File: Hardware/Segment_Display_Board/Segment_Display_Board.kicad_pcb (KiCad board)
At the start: 2 copper layers, 58.4 x 141 mm, 91 parts, among them J101 IN, J102 OUT, J301 USB_B_Micro, J302 PROG, J401 19V Input, J501 Bottom Conn, J502 Top Conn, Q1001 MMBT3904, Q1002 MMBT3906, Q1101 MMBT3904, Q1102 MMBT3906, Q1201 MMBT3904, Q1202 MMBT3906, Q601 MMBT3904, Q602 MMBT3906, Q701 MMBT3904, Q702 MMBT3906, Q801 MMBT3904, Q802 MMBT3906, Q901 MMBT3904, Q902 MMBT3906, SW201 RESET, SW202 DAY_RESET, SW203 DAY_ADV, SW204 DAY_SUB, U201 ATmega328P-A, U202 DS1307Z+, U301 FT232RL, U401 NCV1117ST50T3G, U501 SN74HC595, Y201 16mHz, Y202 32.768kHz

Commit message: Fixup some stuff
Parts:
- R1003, R1103, R1203, R603, R703, R803, R903: value 240R -> 270R
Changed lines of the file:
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@@
       (effects (font (size 0.75 0.75) (thickness 0.15)))
     )
-    (fp_text value "240R" (at 0 2.5) (layer "F.Fab")
+    (fp_text value "270R" (at 0 2.5) (layer "F.Fab")
       (effects (font (size 1 1) (thickness 0.15)))
     )
@@
       (effects (font (size 0.75 0.75) (thickness 0.15)))
     )
-    (fp_text value "240R" (at 0 2.5) (layer "F.Fab")
+    (fp_text value "270R" (at 0 2.5) (layer "F.Fab")
       (effects (font (size 1 1) (thickness 0.15)))
     )
@@
       (effects (font (size 0.75 0.75) (thickness 0.15)))
     )
-    (fp_text value "240R" (at 0 2.5) (layer "F.Fab")
+    (fp_text value "270R" (at 0 2.5) (layer "F.Fab")
       (effects (font (size 1 1) (thickness 0.15)))
     )
@@
       (effects (font (size 0.75 0.75) (thickness 0.15)))
     )
-    (fp_text value "240R" (at 0 2.5) (layer "F.Fab")
+    (fp_text value "270R" (at 0 2.5) (layer "F.Fab")
       (effects (font (size 1 1) (thickness 0.15)))
     )
@@
       (effects (font (size 0.75 0.75) (thickness 0.15)))
     )
-    (fp_text value "240R" (at 0 2.5) (layer "F.Fab")
+    (fp_text value "270R" (at 0 2.5) (layer "F.Fab")
       (effects (font (size 1 1) (thickness 0.15)))
     )
@@
       (effects (font (size 0.75 0.75) (thickness 0.15)))
     )
-    (fp_text value "240R" (at 0 2.5) (layer "F.Fab")
+    (fp_text value "270R" (at 0 2.5) (layer "F.Fab")
       (effects (font (size 1 1) (thickness 0.15)))
     )
@@
       (effects (font (size 0.75 0.75) (thickness 0.15)))
     )
-    (fp_text value "240R" (at 0 2.5) (layer "F.Fab")
+    (fp_text value "270R" (at 0 2.5) (layer "F.Fab")
       (effects (font (size 1 1) (thickness 0.15)))
     )

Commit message: Works enough to do something basic
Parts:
- R1003, R1103, R1203, R603, R703, R803, R903: value 270R -> 680R
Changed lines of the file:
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@@
       (effects (font (size 0.75 0.75) (thickness 0.15)))
     )
-    (fp_text value "270R" (at 0 2.5) (layer "F.Fab")
+    (fp_text value "680R" (at 0 2.5) (layer "F.Fab")
       (effects (font (size 1 1) (thickness 0.15)))
     )
@@
       (effects (font (size 0.75 0.75) (thickness 0.15)))
     )
-    (fp_text value "270R" (at 0 2.5) (layer "F.Fab")
+    (fp_text value "680R" (at 0 2.5) (layer "F.Fab")
       (effects (font (size 1 1) (thickness 0.15)))
     )
@@
       (effects (font (size 0.75 0.75) (thickness 0.15)))
     )
-    (fp_text value "270R" (at 0 2.5) (layer "F.Fab")
+    (fp_text value "680R" (at 0 2.5) (layer "F.Fab")
       (effects (font (size 1 1) (thickness 0.15)))
     )
@@
       (effects (font (size 0.75 0.75) (thickness 0.15)))
     )
-    (fp_text value "270R" (at 0 2.5) (layer "F.Fab")
+    (fp_text value "680R" (at 0 2.5) (layer "F.Fab")
       (effects (font (size 1 1) (thickness 0.15)))
     )
@@
       (effects (font (size 0.75 0.75) (thickness 0.15)))
     )
-    (fp_text value "270R" (at 0 2.5) (layer "F.Fab")
+    (fp_text value "680R" (at 0 2.5) (layer "F.Fab")
       (effects (font (size 1 1) (thickness 0.15)))
     )
@@
       (effects (font (size 0.75 0.75) (thickness 0.15)))
     )
-    (fp_text value "270R" (at 0 2.5) (layer "F.Fab")
+    (fp_text value "680R" (at 0 2.5) (layer "F.Fab")
       (effects (font (size 1 1) (thickness 0.15)))
     )
@@
       (effects (font (size 0.75 0.75) (thickness 0.15)))
     )
-    (fp_text value "270R" (at 0 2.5) (layer "F.Fab")
+    (fp_text value "680R" (at 0 2.5) (layer "F.Fab")
       (effects (font (size 1 1) (thickness 0.15)))
     )

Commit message: Include battery info
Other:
- board text added: "Fits - DL2020 - CR2025 - CR2032"
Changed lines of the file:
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@@
     (effects (font (size 1.5 1.5) (thickness 0.3)))
+  )
+  (gr_text "Fits\n - DL2020\n - CR2025\n - CR2032" (at 143.5 56.5) (layer "F.SilkS")
+    (effects (font (size 1 1) (thickness 0.15)) (justify left))
   )
   (segment (start 127.665 138.335) (end 127.665 130.835) (width 2) (layer "F.Cu") (net 1))

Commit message: Include fancy ICSP programmer (lol)
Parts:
- added J201: Tag Connect, Connector:Tag-Connect_TC2050-IDC-FP_2x05_P1.27mm_Vertical, F.Cu at (147.0, 94.0)
- added JP201: RSTBridge, Jumper:SolderJumper-2_P1.3mm_Bridged_Pad1.0x1.5mm, F.Cu at (139.0, 94.5)
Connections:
- net Net-(D201-Pad2) renamed /MCU/ICSP_SCK
- U201 pad 15: unconnected-(U201-Pad15) -> /MCU/ICSP_MOSI
- U201 pad 16: unconnected-(U201-Pad16) -> /MCU/ICSP_MISO
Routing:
- net /MCU/ICSP_MOSI: track 0.00 -> 23.1 mm, vias 0 -> 2
- net /MCU/ICSP_MISO: track 0.00 -> 15.9 mm, vias 0 -> 2
- net /MCU/ICSP_RST: track 0.00 -> 15.5 mm, vias 0 -> 2
- net /MCU/ICSP_SCK: track 6.80 -> 19.7 mm
- net +5V: track 298.6 -> 306.3 mm, vias 14 -> 15
- net /MCU/RST: track 29.5 -> 37.1 mm
- net GND: track 23.0 -> 24.6 mm, vias 21 -> 33

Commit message: Use new 5in symbol and footprint
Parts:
- removed J501: Bottom Conn, Connector_PinSocket_2.54mm:PinSocket_1x09_P2.54mm_Vertical
- removed J502: Top Conn, Connector_PinSocket_2.54mm:PinSocket_1x09_P2.54mm_Vertical
- added U501: 5inSegment, KenwoodFox:5inSegment, F.Cu at (157.0, 92.0)
- renumbered U501 to U502
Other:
- board text removed: "A"
- board text removed: "B"
- board text removed: "C"
- board text removed: "D"
- board text removed: "DP"
- board text removed: "E"
- board text removed: "F"
- board text removed: "G"
- board text removed: "GND"

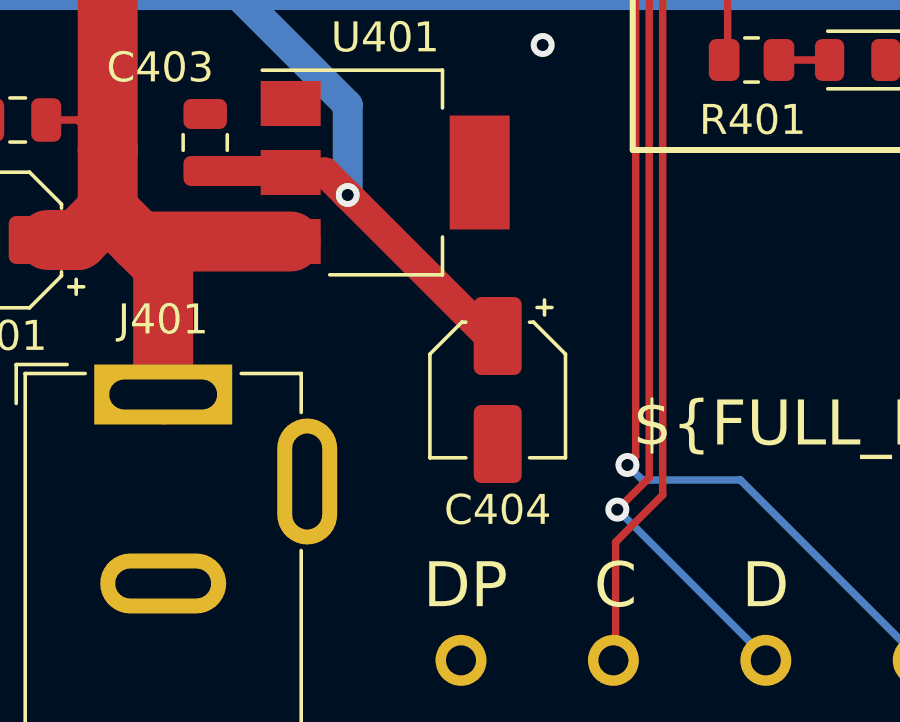
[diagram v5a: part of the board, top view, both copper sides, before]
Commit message: Change package for 1uF capacitor
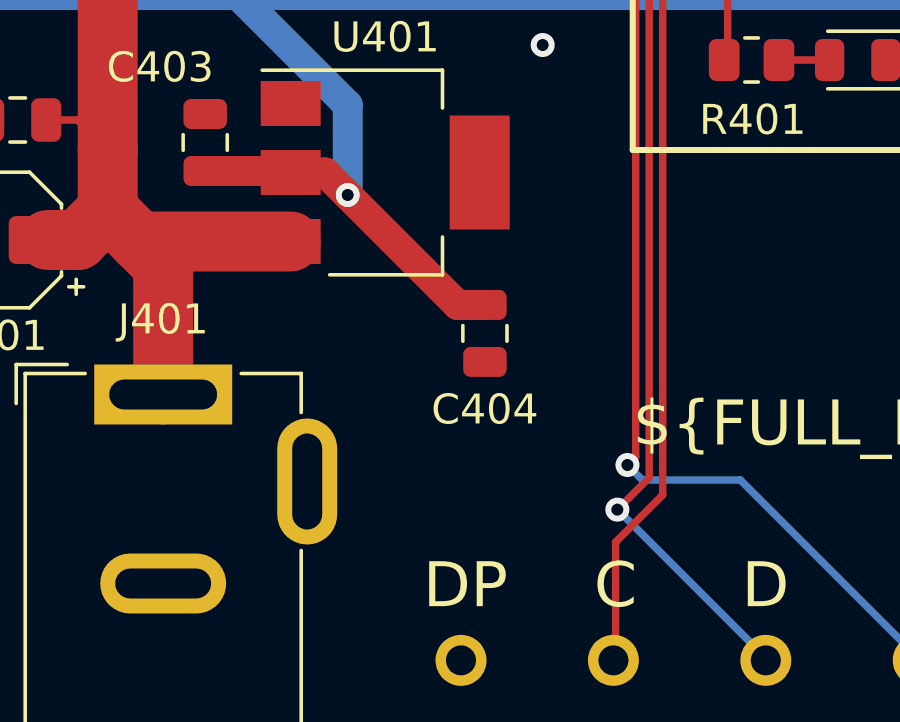
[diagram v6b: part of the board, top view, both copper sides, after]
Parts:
- C404: value 1uf -> 1uF; footprint Capacitor_SMD:CP_Elec_4x3 -> Capacitor_SMD:C_0805_2012Metric
- moved C404 1.93 mm to (147.6, 150.1)
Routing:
- net +5V: track 306.3 -> 305.4 mm
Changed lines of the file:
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@@
       (connect_pads (clearance 0))
       (min_thickness 0.254)
-      (keepout (tracks allowed) (vias not_allowed) (pads allowed ) (copperpour not_allowed) (footprints not_allowed))
+      (keepout (tracks allowed) (vias not_allowed) (pads allowed) (copperpour not_allowed) (footprints not_allowed))
       (fill (thermal_gap 0.508) (thermal_bridge_width 0.508))
       (polygon
@@
     )
   )
+  (footprint "Capacitor_SMD:C_0805_2012Metric" (layer "F.Cu")
+    (at 147.574 150.114 -90)
+    (descr "Capacitor SMD 0805 (2012 Metric), square (rectangular) end terminal, IPC_7351 nominal, (Body size source: IPC-SM-782 page 76, https://www.pcb-3d.com/wordpress/wp-content/uploads/ipc-sm-782a_amendment_1_and_2.pdf, https://docs.google.com/spreadsheets/d/1BsfQQcO9C6DZCsRaXUlFlo91Tg2WpOkGARC1WS5S8t0/edit?usp=sharing), generated with kicad-footprint-generator")
+    (tags "capacitor")
+    (property "Sheetfile" "Power.kicad_sch")
+    (property "Sheetname" "Power")
+    (attr smd)
+    (fp_text reference "C404" (at 2.54 0) (layer "F.SilkS")
+      (effects (font (size 1 1) (thickness 0.15)))
+    )
+    (fp_text value "1uF" (at 0 0 180) (layer "F.Fab")
+      (effects (font (size 1 1) (thickness 0.15)))
+    )
+    (fp_text user "${REFERENCE}" (at 0 0 90) (layer "F.Fab")
+      (effects (font (size 0.5 0.5) (thickness 0.08)))
+    )
+    (fp_line (start -0.261252 0.735) (end 0.261252 0.735) (layer "F.SilkS") (width 0.12))
+    (fp_line (start -0.261252 -0.735) (end 0.261252 -0.735) (layer "F.SilkS") (width 0.12))
+    (fp_line (start 1.7 -0.98) (end 1.7 0.98) (layer "F.CrtYd") (width 0.05))
+    (fp_line (start 1.7 0.98) (end -1.7 0.98) (layer "F.CrtYd") (width 0.05))
+    (fp_line (start -1.7 -0.98) (end 1.7 -0.98) (layer "F.CrtYd") (width 0.05))
+    (fp_line (start -1.7 0.98) (end -1.7 -0.98) (layer "F.CrtYd") (width 0.05))
+    (fp_line (start 1 -0.625) (end 1 0.625) (layer "F.Fab") (width 0.1))
+    (fp_line (start -1 -0.625) (end 1 -0.625) (layer "F.Fab") (width 0.1))
+    (fp_line (start -1 0.625) (end -1 -0.625) (layer "F.Fab") (width 0.1))
+    (fp_line (start 1 0.625) (end -1 0.625) (layer "F.Fab") (width 0.1))
+    (pad "1" smd roundrect (at -0.95 0 270) (size 1 1.45) (layers "F.Cu" "F.Paste" "F.Mask") (roundrect_rratio 0.25)
+      (net 1 "+5V") (pintype "passive"))
+    (pad "2" smd roundrect (at 0.95 0 270) (size 1 1.45) (layers "F.Cu" "F.Paste" "F.Mask") (roundrect_rratio 0.25)
+      (net 2 "GND") (pintype "passive"))
+    (model "${KICAD6_3DMODEL_DIR}/Capacitor_SMD.3dshapes/C_0805_2012Metric.wrl"
+      (offset (xyz 0 0 0))
+      (scale (xyz 1 1 1))
+      (rotate (xyz 0 0 0))
+    )
+  )
   (footprint "Package_TO_SOT_SMD:SOT-23" (layer "F.Cu")
     (at 161.1375 80.4375 -90)
@@
     )
   )
-  (footprint "Capacitor_SMD:CP_Elec_4x3" (layer "F.Cu")
-    (at 148 152 -90)
-    (descr "SMD capacitor, aluminum electrolytic, Nichicon, 4.0x3mm")
-    (tags "capacitor electrolytic")
-    (property "Sheetfile" "Power.kicad_sch")
-    (property "Sheetname" "Power")
-    (attr smd)
-    (fp_text reference "C404" (at 4 0 180) (layer "F.SilkS")
-      (effects (font (size 1 1) (thickness 0.15)))
-    )
-    (fp_text value "1uf" (at 0 0 180) (layer "F.Fab")
-      (effects (font (size 1 1) (thickness 0.15)))
-    )
-    (fp_text user "${REFERENCE}" (at 0 0 90) (layer "F.Fab")
-      (effects (font (size 0.8 0.8) (thickness 0.12)))
-    )
-    (fp_line (start -2.26 1.195563) (end -1.195563 2.26) (layer "F.SilkS") (width 0.12))
-    (fp_line (start 2.26 2.26) (end 2.26 1.06) (layer "F.SilkS") (width 0.12))
-    (fp_line (start -2.26 1.195563) (end -2.26 1.06) (layer "F.SilkS") (width 0.12))
-    (fp_line (start -2.75 -1.81) (end -2.75 -1.31) (layer "F.SilkS") (width 0.12))
-    (fp_line (start -3 -1.56) (end -2.5 -1.56) (layer "F.SilkS") (width 0.12))
-    (fp_line (start -2.26 -1.195563) (end -2.26 -1.06) (layer "F.SilkS") (width 0.12))
-    (fp_line (start -1.195563 2.26) (end 2.26 2.26) (layer "F.SilkS") (width 0.12))
-    (fp_line (start -2.26 -1.195563) (end -1.195563 -2.26) (layer "F.SilkS") (width 0.12))
-    (fp_line (start 2.26 -2.26) (end 2.26 -1.06) (layer "F.SilkS") (width 0.12))
-    (fp_line (start -1.195563 -2.26) (end 2.26 -2.26) (layer "F.SilkS") (width 0.12))
-    (fp_line (start -2.4 -1.25) (end -1.25 -2.4) (layer "F.CrtYd") (width 0.05))
-    (fp_line (start -2.4 -1.05) (end -3.35 -1.05) (layer "F.CrtYd") (width 0.05))
-    (fp_line (start -1.25 -2.4) (end 2.4 -2.4) (layer "F.CrtYd") (width 0.05))
-    (fp_line (start -3.35 1.05) (end -2.4 1.05) (layer "F.CrtYd") (width 0.05))
-    (fp_line (start 3.35 1.05) (end 2.4 1.05) (layer "F.CrtYd") (width 0.05))
-    (fp_line (start -2.4 -1.25) (end -2.4 -1.05) (layer "F.CrtYd") (width 0.05))
-    (fp_line (start 3.35 -1.05) (end 3.35 1.05) (layer "F.CrtYd") (width 0.05))
-    (fp_line (start 2.4 -2.4) (end 2.4 -1.05) (layer "F.CrtYd") (width 0.05))
-    (fp_line (start -2.4 1.25) (end -1.25 2.4) (layer "F.CrtYd") (width 0.05))
-    (fp_line (start -2.4 1.05) (end -2.4 1.25) (layer "F.CrtYd") (width 0.05))
-    (fp_line (start 2.4 -1.05) (end 3.35 -1.05) (layer "F.CrtYd") (width 0.05))
-    (fp_line (start 2.4 1.05) (end 2.4 2.4) (layer "F.CrtYd") (width 0.05))
-    (fp_line (start -3.35 -1.05) (end -3.35 1.05) (layer "F.CrtYd") (width 0.05))
-    (fp_line (start -1.25 2.4) (end 2.4 2.4) (layer "F.CrtYd") (width 0.05))
-    (fp_line (start -2.15 -1.15) (end -2.15 1.15) (layer "F.Fab") (width 0.1))
-    (fp_line (start -1.574773 -1) (end -1.174773 -1) (layer "F.Fab") (width 0.1))
-    (fp_line (start -2.15 1.15) (end -1.15 2.15) (layer "F.Fab") (width 0.1))
-    (fp_line (start 2.15 -2.15) (end 2.15 2.15) (layer "F.Fab") (width 0.1))
-    (fp_line (start -1.374773 -1.2) (end -1.374773 -0.8) (layer "F.Fab") (width 0.1))
-    (fp_line (start -1.15 -2.15) (end 2.15 -2.15) (layer "F.Fab") (width 0.1))
-    (fp_line (start -2.15 -1.15) (end -1.15 -2.15) (layer "F.Fab") (width 0.1))
-    (fp_line (start -1.15 2.15) (end 2.15 2.15) (layer "F.Fab") (width 0.1))
-    (fp_circle (center 0 0) (end 2 0) (layer "F.Fab") (width 0.1) (fill none))
-    (pad "1" smd roundrect (at -1.8 0 270) (size 2.6 1.6) (layers "F.Cu" "F.Paste" "F.Mask") (roundrect_rratio 0.15625)
-      (net 1 "+5V") (pintype "passive"))
-    (pad "2" smd roundrect (at 1.8 0 270) (size 2.6 1.6) (layers "F.Cu" "F.Paste" "F.Mask") (roundrect_rratio 0.15625)
-      (net 2 "GND") (pintype "passive"))
-    (model "${KICAD6_3DMODEL_DIR}/Capacitor_SMD.3dshapes/CP_Elec_4x3.wrl"
-      (offset (xyz 0 0 0))
-      (scale (xyz 1 1 1))
-      (rotate (xyz 0 0 0))
-    )
-  )
   (footprint "Capacitor_SMD:C_0805_2012Metric" (layer "F.Cu")
     (at 117.25 40 180)
@@
   (segment (start 139.6 112.1) (end 139 111.5) (width 0.25) (layer "F.Cu") (net 1))
   (segment (start 118.0625 35) (end 118.0625 32.75) (width 0.25) (layer "F.Cu") (net 1))
+  (segment (start 146.664 149.164) (end 147.574 149.164) (width 1) (layer "F.Cu") (net 1))
   (segment (start 143.8375 46.4825) (end 143.225 47.095) (width 0.25) (layer "F.Cu") (net 1))
-  (segment (start 143 145.5) (end 147.7 150.2) (width 1) (layer "F.Cu") (net 1))
   (segment (start 127.85 45.775) (end 128.775 45.775) (width 0.25) (layer "F.Cu") (net 1))
   (segment (start 159.925 129.9875) (end 159.925 130.925) (width 0.25) (layer "F.Cu") (net 1))
@@
   (segment (start 141.2 113.7) (end 139 111.5) (width 0.25) (layer "F.Cu") (net 1))
   (segment (start 128.725 106.5) (end 128.5 106.5) (width 0.25) (layer "F.Cu") (net 1))
+  (segment (start 143 145.5) (end 146.664 149.164) (width 1) (layer "F.Cu") (net 1))
   (segment (start 145.73 93.365) (end 145.73 92.77) (width 0.25) (layer "F.Cu") (net 1))
   (segment (start 118.775199 42.525) (end 120.65 42.525) (width 0.25) (layer "F.Cu") (net 1))
@@
   (segment (start 155.665 140.885) (end 155.665 138.335) (width 0.25) (layer "F.Cu") (net 1))
   (segment (start 141.2 114.75) (end 141.2 113.7) (width 0.25) (layer "F.Cu") (net 1))
-  (segment (start 147.7 150.2) (end 148 150.2) (width 1) (layer "F.Cu") (net 1))
   (segment (start 158.9625 129.9875) (end 157.95 131) (width 0.25) (layer "F.Cu") (net 1))
   (segment (start 128.5 106.275) (end 128.725 106.5) (width 0.25) (layer "F.Cu") (net 1))

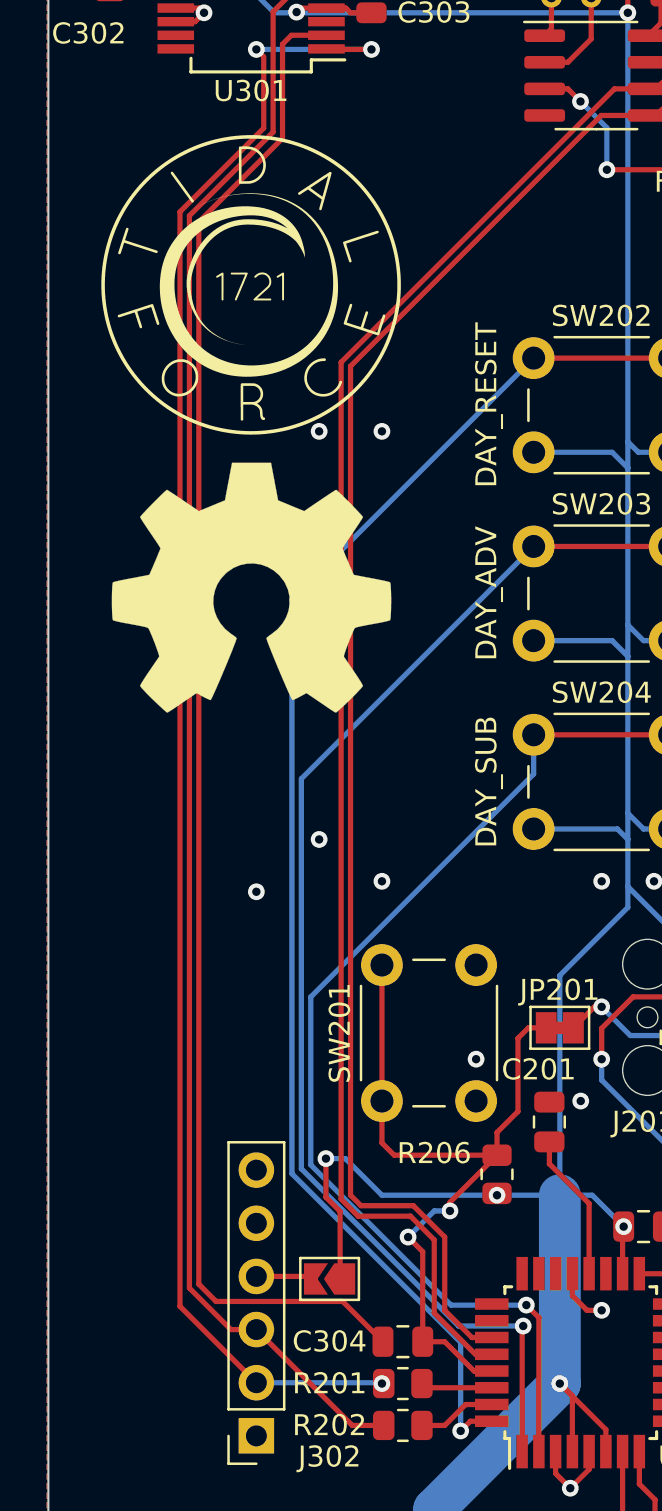
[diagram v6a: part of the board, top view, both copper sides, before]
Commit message: Add breakout for external buttons
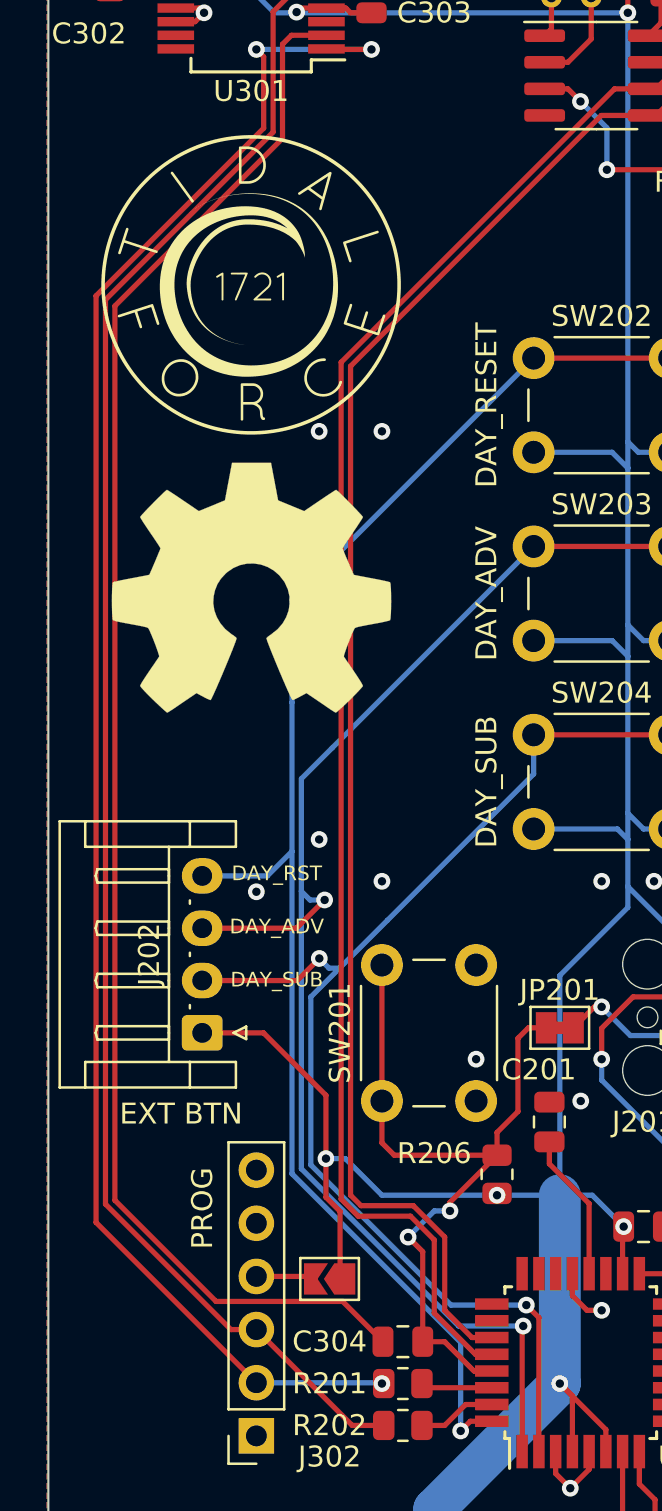
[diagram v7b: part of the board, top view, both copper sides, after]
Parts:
- added J202: EXT BTN, Connector_JST:JST_EH_S4B-EH_1x04_P2.50mm_Horizontal, F.Cu at (121.9, 94.7)
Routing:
- net +5V: track 305.4 -> 315.6 mm
- net /MCU/DAY_ADVANCE: track 63.0 -> 70.7 mm, vias 1 -> 2
- net /MCU/DAY_SUBTRACT: track 54.2 -> 61.4 mm, vias 1 -> 2
- net /MCU/DAY_RESET: track 70.0 -> 75.0 mm
- net Net-(C304-Pad2): track 73.1 -> 76.4 mm
- net /MCU/RXD: track 80.8 -> 84.1 mm
- net /MCU/TXD: track 77.5 -> 80.9 mm
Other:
- board text added: "DAY_ADV"
- board text added: "DAY_RST"
- board text added: "DAY_SUB"
